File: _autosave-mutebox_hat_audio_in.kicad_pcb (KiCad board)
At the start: 2 copper layers, 65 x 56 mm, 52 parts, among them J1 GPIO, J2 PLR237/T10BK, J3 RCJ-042, J4 RCJ-042, U2 74LVC157, U3 PCM1862DBT, U5 DIR9001PW, Y3 XO32

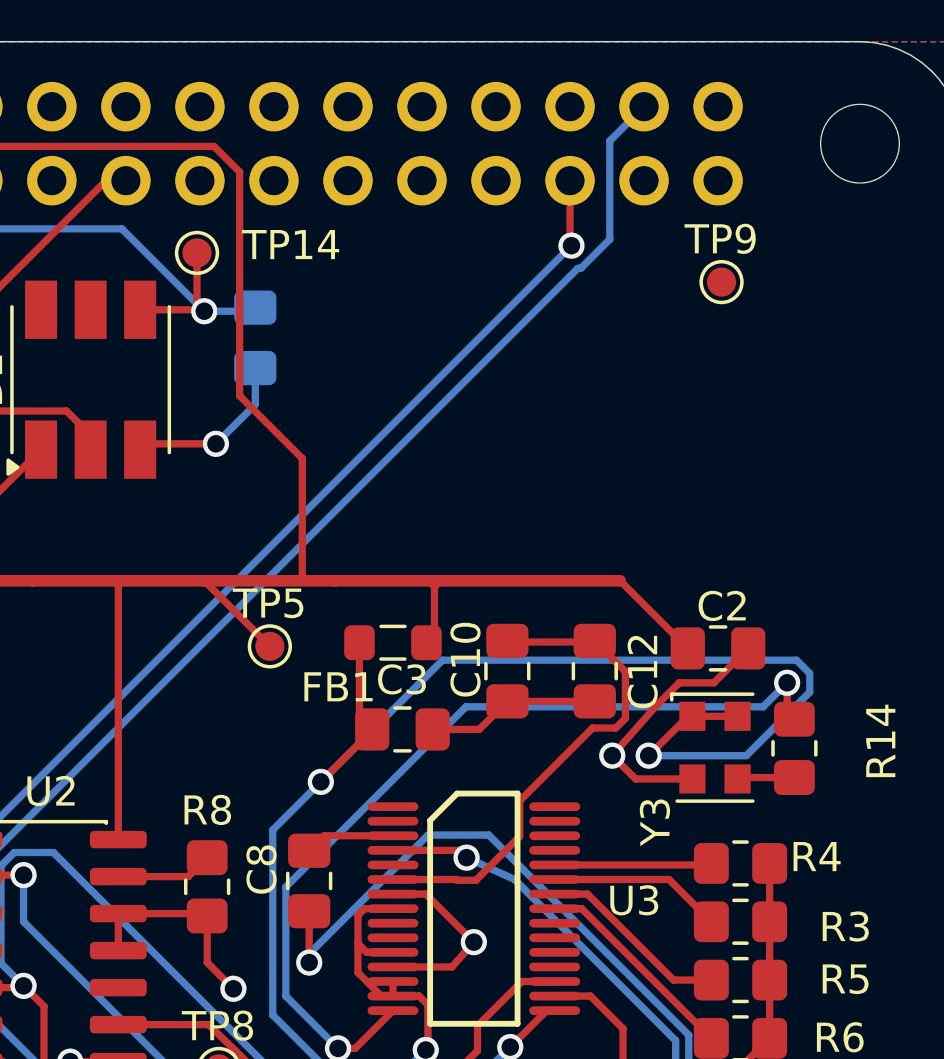
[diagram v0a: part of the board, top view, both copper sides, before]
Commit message: Added testpoint with large clip on footprint
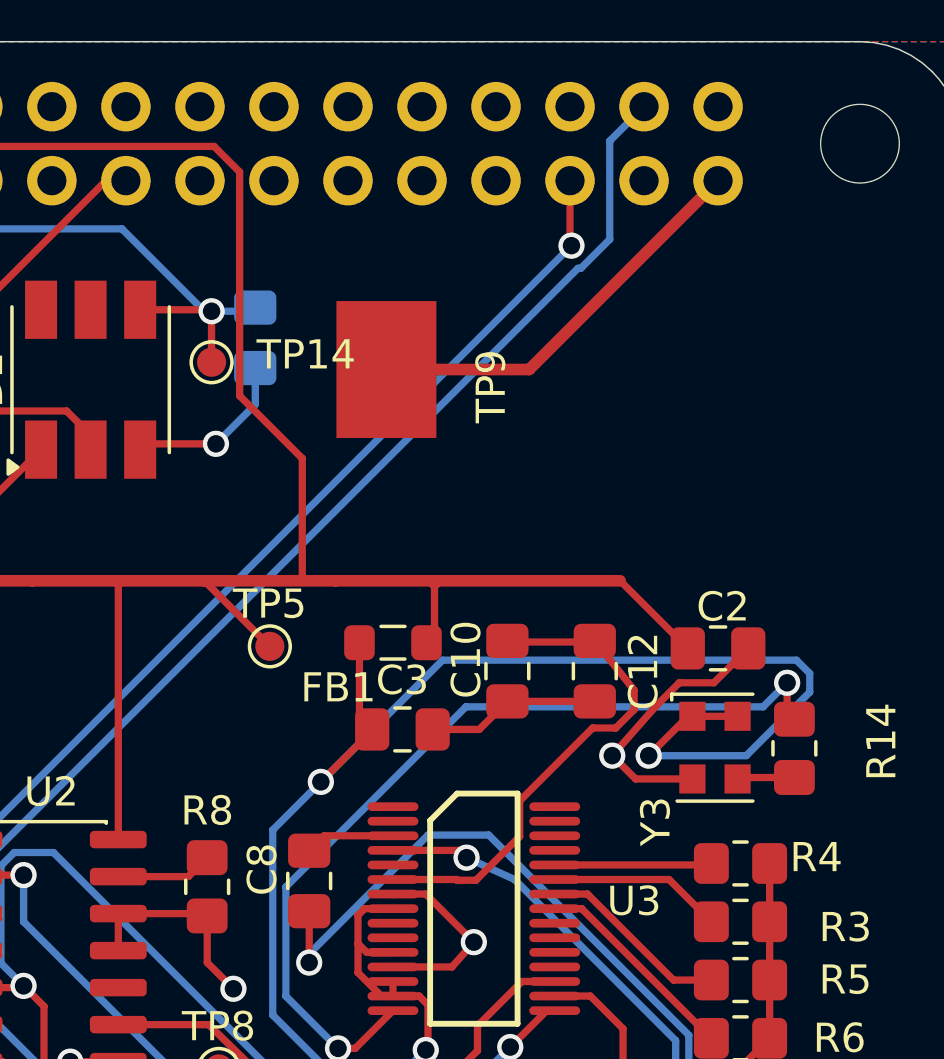
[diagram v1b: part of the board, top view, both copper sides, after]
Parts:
- TP9: value TP_GND -> 5016; footprint TestPoint:TestPoint_Pad_D1.0mm -> Connector:KEYSTONE_5016
- moved TP9 11.9 mm to (145.2, 55.2), turned to -90 degrees
- moved TP14 3.78 mm to (139.2, 55.0)
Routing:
- net GND: track 139.3 -> 153.4 mm
